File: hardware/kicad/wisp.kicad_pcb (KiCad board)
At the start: 2 copper layers, 140 x 100 mm, 73 parts, among them J1 USB-C, J2 Second I2C Bus, J3 mmWave UART (LD2410), J4 I2S Mic (INMP441), J5 Switched DC Output, J6 Reed/Hall Contact, J7 1-Wire Bus, J8 Analog Sensor Pad, J9 Expansion Header, Q1 MMBT3904, Q2 MMBT3904, Q3 2N7002, Q4 MMBT3904, SW1 RESET, SW2 BOOT, U1 CH340C, U2 AP63203WU-7, U3 ESP32-WROOM-32, U4 SCD41-D-R2, U5 BME680, U6 BH1750FVI-TR

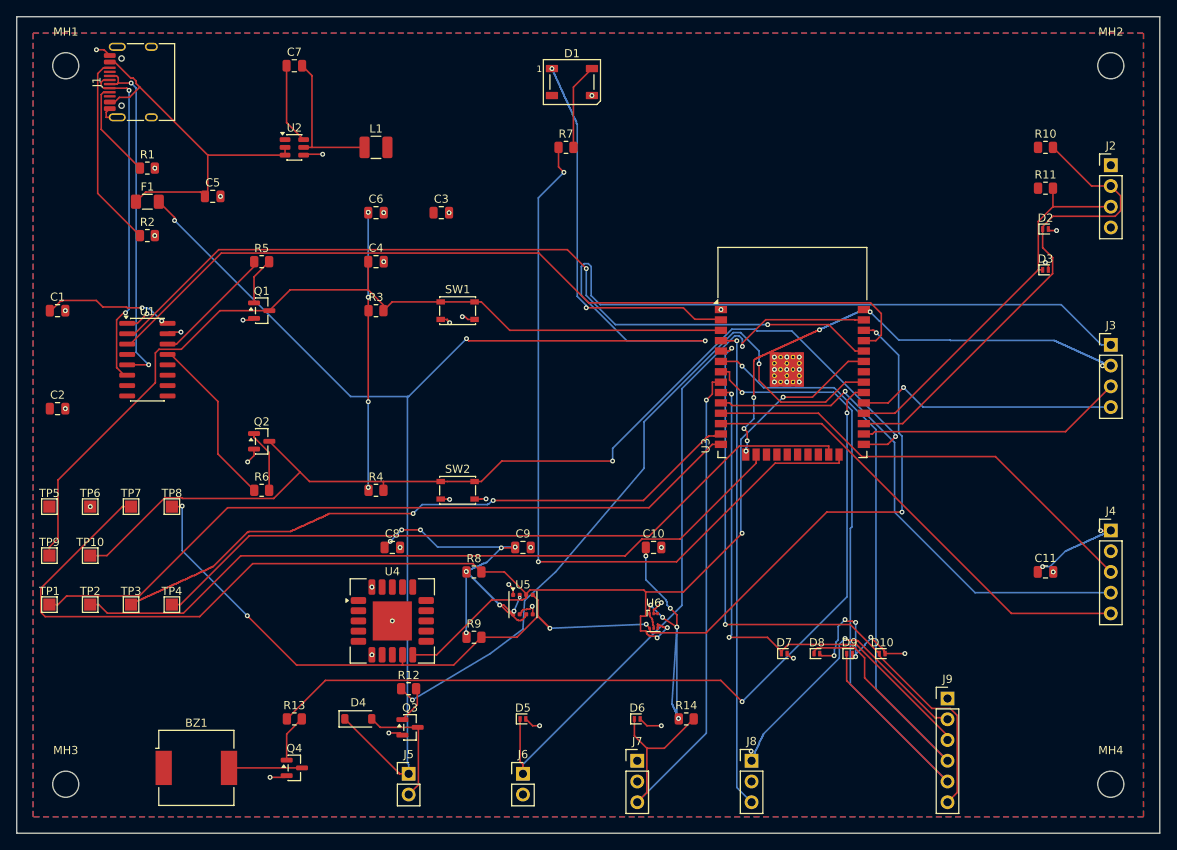
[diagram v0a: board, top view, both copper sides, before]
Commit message: Compact PCB layout: 140x100mm -> 75x80mm
Repositioned all 73 footprints into denser functional zones, moved
roughly half the passives/small-signal parts to the back copper layer,
and re-routed from scratch with Freerouting (all 44 nets, 0 unrouted).

- Shrunk U3's (ESP32-WROOM-32) own courtyard from 48x41mm to 19x27mm:
  the imported footprint applied the 15mm Espressif antenna keepout
  symmetrically around the whole module instead of just the antenna
  side. The 15mm clearance now lives on its own dedicated 26x16mm
  keepout zone above the antenna edge instead.
- Fixed undersized (0.15mm) track segments left by the autorouter.
- Reduced/hid silkscreen text to resolve overlap findings on the
  denser board; added a silkscreen identification line.
- Regenerated Gerbers, drill file, and prototype CPL.

Known remaining issue before this is fab-ready: 26 GND/+3V3 pads have
lost pour connectivity where the copper fill fragmented around tightly
packed clusters. Documented in hardware/README.md together with two
DRC findings that read as false positives (verified via pad
coordinates). See follow-up issue for the stitching fix.

Co-Authored-By: Claude Sonnet 5 <noreply@anthropic.com>
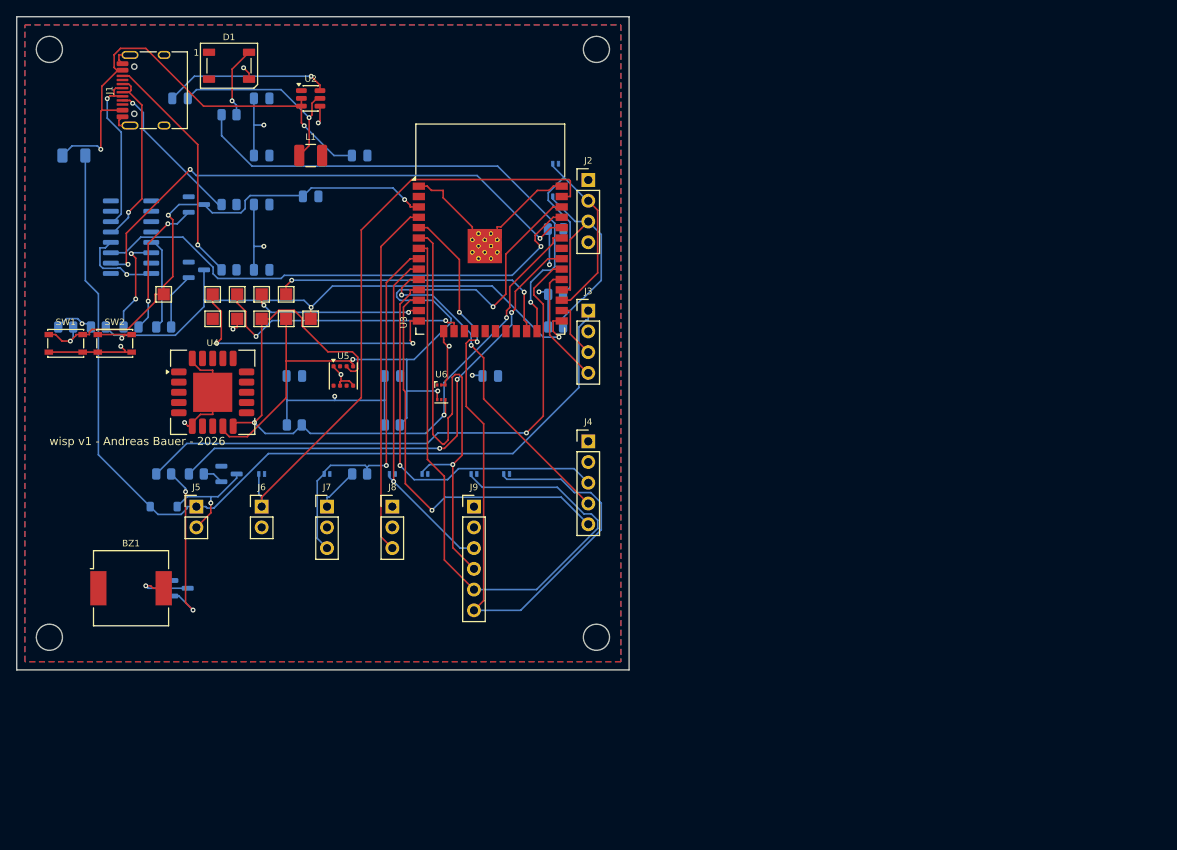
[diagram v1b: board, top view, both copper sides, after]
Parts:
- C1, C10, C11, C2, C3, C4, C5, C6, C7, C8, C9, D10, D2, D3, D4, D5, D6, D7, D8, D9, F1, Q1, Q2, Q3, Q4, R1, R10, R11, R12, R13, R14, R2, R3, R4, R5, R6, R7, R8, R9, U1: moved to B.Cu
- moved C11 73.2 mm to (66.0, 26.0)
- moved MH4 65.5 mm to (71.0, 76.0)
- moved J4 64.9 mm to (70.0, 52.0)
- moved J3 64.1 mm to (70.0, 36.0)
- moved J2 64.0 mm to (70.0, 20.0)
- moved MH2 63.0 mm to (71.0, 4.00)
- moved R10 62.6 mm to (66.0, 34.0)
- moved J9 62.6 mm to (56.0, 60.0)
- moved R11 62.4 mm to (66.0, 38.0)
- moved D3 60.7 mm to (66.0, 22.0)
- moved D2 60.5 mm to (66.0, 18.0)
- moved J8 53.9 mm to (46.0, 60.0)
- moved D7 52.8 mm to (46.0, 56.0)
- moved D8 52.8 mm to (50.0, 56.0)
- moved D10 51.0 mm to (60.0, 56.0)
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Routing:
- net +3V3: track 246.4 -> 73.8 mm, vias 28 -> 8
- net /+5V_EXT: track 229.2 -> 116.0 mm, vias 3 -> 0
- net /SDA: track 171.7 -> 90.0 mm, vias 4 -> 3
- net /JTAG_TMS: track 81.0 -> 20.9 mm
- net /JTAG_TCK: track 90.7 -> 32.3 mm, vias 0 -> 2
- net /JTAG_TDI: track 90.4 -> 34.6 mm, vias 0 -> 2
- net /JTAG_TDO: track 89.5 -> 36.0 mm, vias 0 -> 2
- net /IO0: track 128.3 -> 75.8 mm, vias 2 -> 3
- net GND: track 127.3 -> 74.8 mm, vias 60 -> 7
- net /SCL: track 141.9 -> 94.3 mm, vias 6 -> 3
- net /EN: track 109.3 -> 64.5 mm, vias 0 -> 3
- net /CH_RXD: track 105.1 -> 63.5 mm, vias 0 -> 1
- net /CH_TXD: track 101.6 -> 66.7 mm, vias 2 -> 3
- net /BUZZER_CTRL: track 103.4 -> 70.8 mm, vias 2 -> 1
- net /LED_CTRL: track 95.2 -> 63.2 mm, vias 2 -> 1
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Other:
- board size 140 x 100 mm -> 75 x 80 mm
- board text added: "wisp v1 - Andreas Bauer - 2026"

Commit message: Investigate GND/+3V3 pour-stitch gaps (#8), close 1 of 26 with verified routing
Ran three independent, real-DRC-verified approaches to close the 26
GND/+3V3 unconnected pour-fill islands from #8:

- Freerouting on the de-planed full nets: consistently plateaus at
  16+ unrouted connections regardless of pass count -- congestion,
  not a pass-budget problem.
- Collision-checked candidate-pair search between disconnected copper
  islands (KiCad's own SHAPE_SEGMENT::Collide/GetClearance, not a
  distance heuristic): finds zero viable straight-line path for most
  gaps at any clearance down to 0mm -- direct paths physically overlap
  other nets' copper, they don't just fail clearance.
- Nudge-and-verify (bend the one blocking trace out of the way, then
  re-verify everything including the moved trace against the new
  stitch): closed 1 gap. An earlier version of this had a real
  validation bug -- it excluded a blocker from the obstacle set once
  removed but never added its replacement geometry, so a stitch could
  be "verified" against a world where the blocker's bent replacement
  didn't yet exist. Fixed; the honest success count dropped from a
  false 17 to a verified 1.

25 of 26 gaps remain and, per this investigation, need a placement/
routing layout change rather than more automated stitching -- documented
in hardware/README.md alongside what was tried and why.

Gerbers/drill regenerated from the updated board. BOM/CPL unchanged
(no parts moved).

Co-Authored-By: Claude Sonnet 5 <noreply@anthropic.com>
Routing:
- net GND: track 74.8 -> 75.6 mm
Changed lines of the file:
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@@
+	)
+	(segment
+		(start 44.652058 42.697465)
+		(end 45.44533 42.697465)
+		(width 0.2)
+		(layer "B.Cu")
+		(net "GND")
 	)
 	(segment

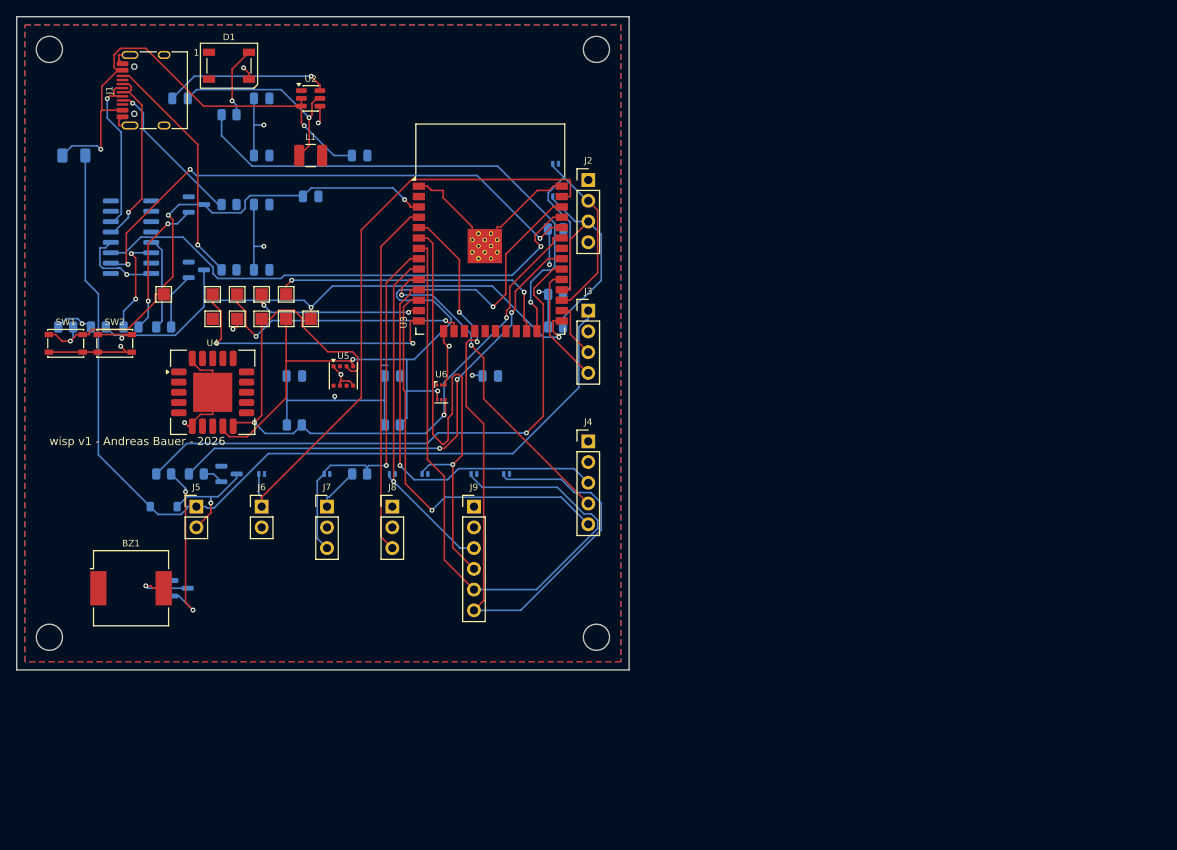
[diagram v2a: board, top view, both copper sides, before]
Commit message: Grow board to 100x100mm to close most GND/+3V3 pour-stitch gaps
Follow-up to #8/#9, which concluded the remaining 25 of 26 unconnected
GND/+3V3 pour islands at 75x80mm needed a placement change, not more
routing cleverness. Grew the outline to 100x100mm (JLCPCB's cheapest
prototype price bracket ceiling, no cost increase), proportionally
repositioned all 73 footprints, and re-routed from scratch with
Freerouting.

Caught and fixed a real bug along the way: naively scaling U3's antenna
keepout zone (not footprint-owned, so it doesn't move automatically)
double-transformed it relative to U3, which kicad-cli pcb drc exposed as
geometrically impossible courtyard-overlap violations against components
~50mm away. Fixed by translating the keepout by U3's exact movement
delta instead of scaling it.

Re-ran the same collision-checked stitching method from #9 against the
regrown board: closed 2 more islands directly, verified with zero new
clearance/shorting_items findings. Fixed two real regressions from the
regrow (D2 partially inside the antenna keepout, 7 sub-minimum-width
Freerouting stub tracks) and one cosmetic one (title text silkscreen
overlap).

Result: 13 of 26 original gaps remain (down from 25), on GND pads of
D3/D6/D9 and +3V3 pads of U2/U5/U6. Still not fab-ready -- these are
real floating references, not cosmetic -- but the corridor for closing
them is now a handful of specific congested signal nets instead of a
placement-density wall. Full writeup in hardware/README.md.

Gerbers/drill/CPL regenerated from the updated board; BOM unchanged (no
parts added or removed).

Co-Authored-By: Claude Sonnet 5 <noreply@anthropic.com>
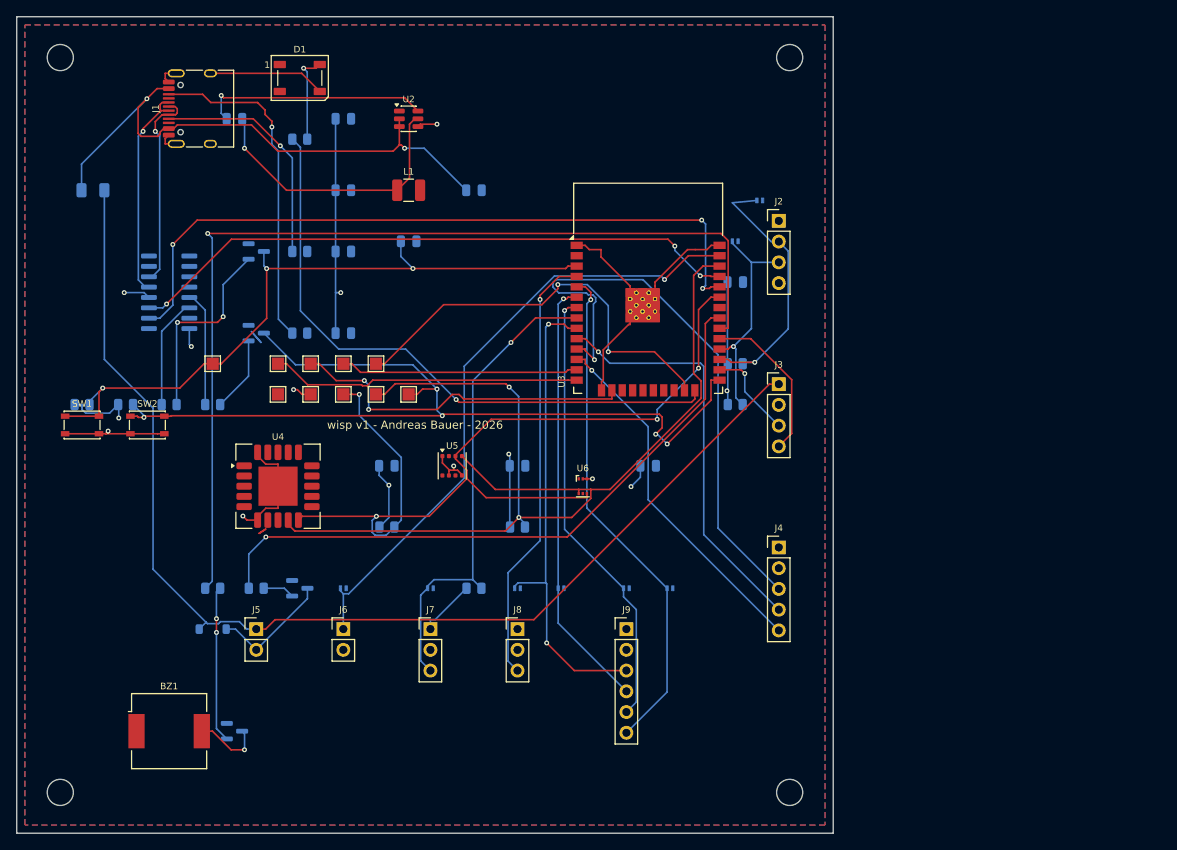
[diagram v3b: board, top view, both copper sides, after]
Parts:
- moved MH4 30.3 mm to (94.7, 95.0)
- moved J4 26.7 mm to (93.3, 65.0)
- moved D2 25.4 mm to (91.0, 22.5)
- moved J3 25.0 mm to (93.3, 45.0)
- moved D10 24.4 mm to (80.0, 70.0)
- moved R11 24.0 mm to (88.0, 47.5)
- moved J9 23.9 mm to (74.7, 75.0)
- moved J2 23.9 mm to (93.3, 25.0)
- moved MH2 23.7 mm to (94.7, 5.00)
- moved R10 23.6 mm to (88.0, 42.5)
- moved D9 23.3 mm to (74.7, 70.0)
- moved C11 22.9 mm to (88.0, 32.5)
- moved D3 22.7 mm to (88.0, 27.5)
- moved C10 22.2 mm to (77.3, 55.0)
- moved D8 21.8 mm to (66.7, 70.0)
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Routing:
- net /BUZZER_CTRL: track 70.8 -> 119.9 mm
- net /IO0: track 75.8 -> 114.4 mm, vias 3 -> 5
- net /SCL: track 94.3 -> 130.8 mm, vias 3 -> 2
- net /EXP_IO35: track 82.5 -> 55.0 mm, vias 0 -> 1
- net /EXP_IO39: track 89.8 -> 62.3 mm, vias 2 -> 1
- net /+5V_EXT: track 116.0 -> 142.4 mm
- net /MIC_WS: track 48.1 -> 72.9 mm
- net GND: track 75.6 -> 99.5 mm, vias 7 -> 6
- net /SDA: track 90.0 -> 113.8 mm, vias 3 -> 4
- net /CH_TXD: track 66.7 -> 87.9 mm
- net /EN: track 64.5 -> 84.5 mm
- net /SW_OUT_CTRL: track 62.8 -> 79.2 mm, vias 3 -> 1
- net /EXP_IO33: track 42.3 -> 58.3 mm, vias 1 -> 2
- net /JTAG_TDO: track 36.0 -> 51.4 mm
- net /EXP_IO34: track 66.7 -> 53.5 mm
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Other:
- board size 75 x 80 mm -> 100 x 100 mm

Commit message: Close 19 of 26 GND/+3V3 pour-stitch gaps with layer-hop and A* stitching
Follow-up to the 100x100mm regrow, which left 13 of 26 gaps blocked by
same-layer signal traces that a same-layer nudge can't route around
without moving the blocker. Two more collision-verified techniques,
applied in order:

- Layer-hop stitching: route the stitch itself onto the opposite copper
  layer for just the colliding segment, via-hopping back down past the
  blocker, instead of moving the blocker. Standard 0.6mm/0.3mm vias
  except directly under U5, which reuses the existing DRU via-size
  exception (0.45mm/0.2mm) since standard vias don't fit its 0.8mm pitch.
  Closed 6 islands.
- A* pathfinding for the rest: grid-based search with the same real
  KiCad-collision checker, finding genuine multi-waypoint detours around
  long obstructions (e.g. /+5V_EXT crossing most of a board quadrant)
  instead of a single bent segment. Caught and fixed a real bug along the
  way -- the pathfinder's obstacle set didn't include keepout rule areas,
  so an early run routed a stitch straight through U3's antenna keepout;
  fixed by adding zone outlines to the obstacle collision set. Closed 1
  more island after the fix.

Result: 6 of 26 original gaps remain (D9's GND pad, U5 pads 2/6, U6 pads
1/5), all on sub-1mm-pitch IC pins where standard vias/traces have no
room even on the regrown board. Verified exhaustively -- direct stitch,
nudge, layer-hop, and A* (up to 60mm search radius) all independently
converge on the same 6 pads with zero viable path. Closing them needs
hand-placed vias-in-pad or a further board regrow, not more scripted
search.

kicad-cli pcb drc --severity-all: 7 violations, all pre-existing accepted
false-positive/cosmetic categories, zero clearance/shorting_items.
Gerbers/drill regenerated; BOM/CPL unchanged (no footprints moved this
pass).

Co-Authored-By: Claude Sonnet 5 <noreply@anthropic.com>
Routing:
- net GND: track 99.5 -> 291.6 mm, vias 6 -> 22
- net +3V3: track 85.4 -> 86.2 mm, vias 8 -> 10
